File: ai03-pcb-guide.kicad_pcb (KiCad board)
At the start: 2 copper layers, 169.9 x 69.8 mm, 34 parts, among them J1 USB_mini_micro_B, SW1 SW_Push, U1 ATmega32U4-AU, Y1 Crystal_GND24_Small

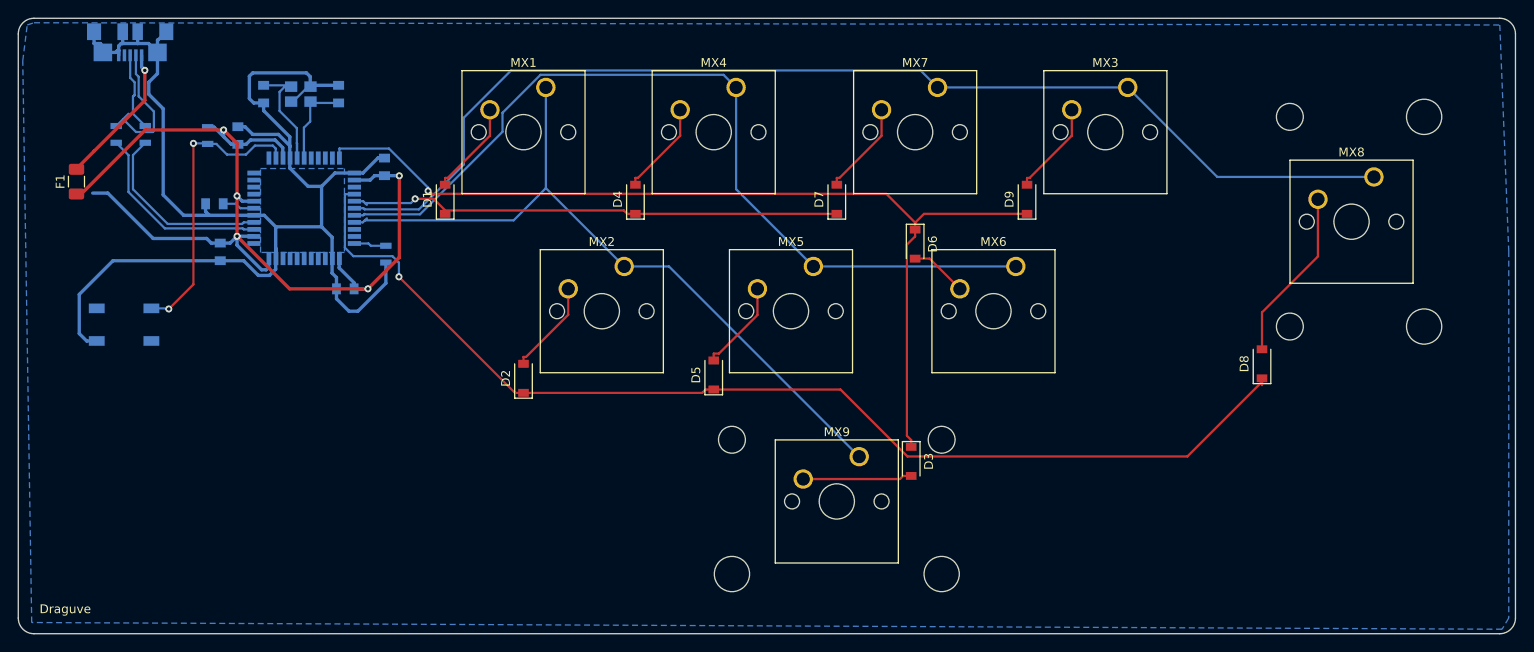
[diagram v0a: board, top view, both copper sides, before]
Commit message: using pro micro instead,added tht diodes,firmware
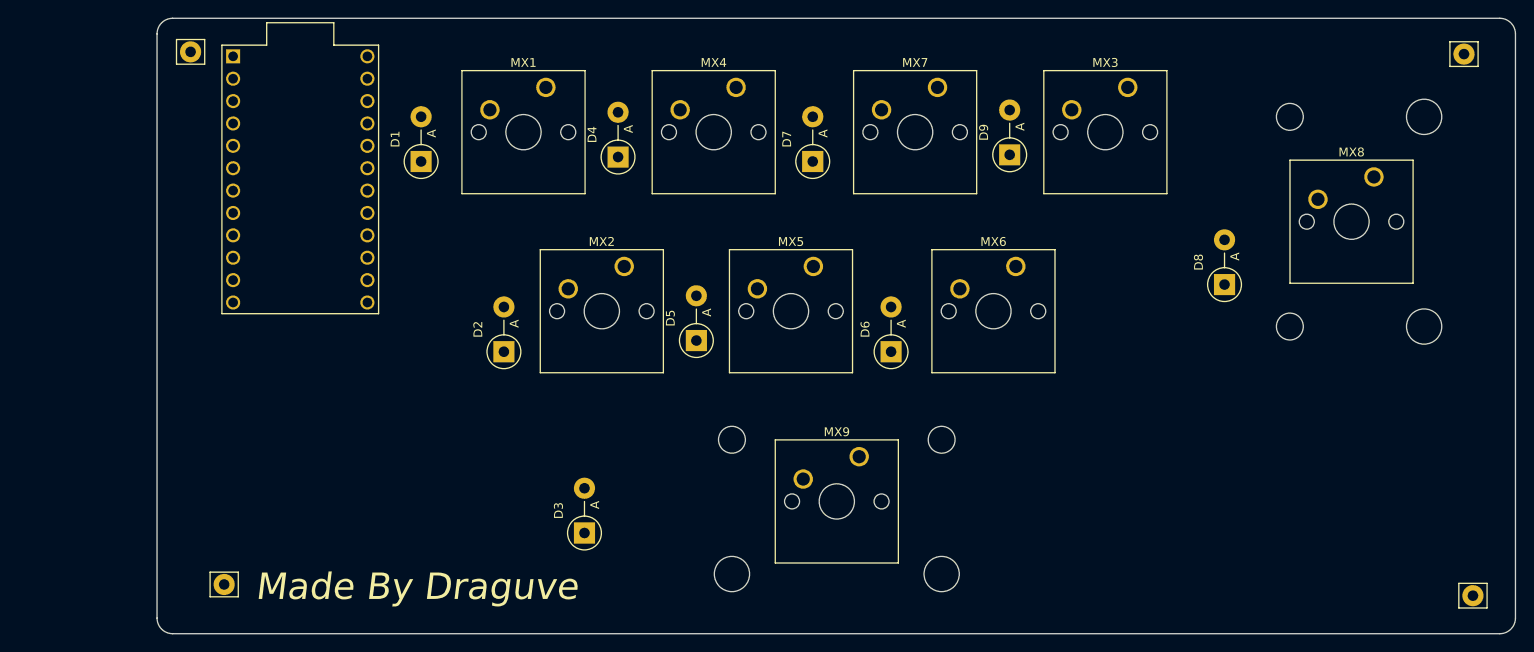
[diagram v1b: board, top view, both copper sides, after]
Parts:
- removed C1, C2, C5: 0.1uF, Capacitors_SMD:C_0805
- removed C3, C4: 22pF, Capacitors_SMD:C_0805
- removed C6: 1uF, Capacitors_SMD:C_0805
- removed C7: 10uF, Capacitors_SMD:C_0805
- removed F1: 500mA, Fuse:Fuse_1206_3216Metric
- removed J1: USB_mini_micro_B, keyboard_parts:USB_microB
- removed R1, R2: 22, Resistors_SMD:R_0805
- removed R3, R4: 10k, Resistors_SMD:R_0805
- removed SW1: SW_Push, random-keyboard-parts:SKQG-1155865
- removed Y1: Crystal_GND24_Small, Crystals:Crystal_SMD_3225-4pin_3.2x2.5mm
- added ?: , Connector_Pin:Pin_D1.2mm_L11.3mm_W3.0mm_Flat, F.Cu at (190.6, 64.8)
- added ?: , Connector_Pin:Pin_D1.2mm_L11.3mm_W3.0mm_Flat, F.Cu at (191.6, 126.3)
- added ?: , Connector_Pin:Pin_D1.2mm_L11.3mm_W3.0mm_Flat, F.Cu at (49.8, 125.0)
- added ?: , Connector_Pin:Pin_D1.2mm_L11.3mm_W3.0mm_Flat, F.Cu at (46.0, 64.5)
- D1, D2, D3, D4, D5, D6, D7, D8, D9: footprint Diode_SMD:D_SOD-123 -> Diode_THT:D_DO-15_P5.08mm_Vertical_AnodeUp
- U1: value ATmega32U4-AU -> ProMicro; footprint Housings_QFP:TQFP-44_10x10mm_Pitch0.8mm -> promicro:ProMicro; moved to F.Cu
- moved D3 38.0 mm to (90.7, 119.2), turned to 90 degrees
- moved D6 12.5 mm to (125.5, 98.6), turned to 90 degrees
- moved D8 9.95 mm to (163.4, 91.0)
- moved D9 5.42 mm to (139.0, 76.2)
- moved D4 5.19 mm to (94.6, 76.5)
- moved D1 5.09 mm to (72.2, 77.0)
- moved D7 5.09 mm to (116.6, 77.0)
- moved D5 4.38 mm to (103.4, 97.3)
- moved D2 3.75 mm to (81.6, 98.6)
- moved U1 3.30 mm to (58.5, 79.0), turned to 270 degrees
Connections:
- U1 pad 14: +5V -> COL2
- U1 pad 15: GND -> COL1
- U1 pad 16: Net-(C4-Pad1) -> COL0
- U1 pad 18: Net-(U1-Pad18) -> ROW2
- U1 pad 19: Net-(U1-Pad19) -> ROW1
- U1 pad 2: +5V -> Net-(U1-Pad2)
- U1 pad 20: Net-(U1-Pad20) -> ROW0
- U1 pad 22: ROW2 -> Net-(U1-Pad22)
- U1 pad 23: GND -> Net-(U1-Pad23)
- U1 pad 24: +5V -> Net-(U1-Pad24)
- U1 pad 5: GND -> Net-(U1-Pad5)
- U1 pad 7: +5V -> Net-(U1-Pad7)
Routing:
- net GND: track 163.8 -> 0.00 mm
- net COL2: track 130.4 -> 0.00 mm
- net ROW1: track 126.6 -> 0.00 mm, vias 1 -> 0
- net +5V: track 118.6 -> 0.00 mm, vias 5 -> 0
- net ROW2: track 109.3 -> 0.00 mm, vias 1 -> 0
- net COL1: track 98.8 -> 0.00 mm
- net COL0: track 83.3 -> 0.00 mm
- net ROW0: track 56.5 -> 0.00 mm, vias 1 -> 0
- net Net-(U1-Pad13): track 34.0 -> 0.00 mm, vias 2 -> 0
- net Net-(U1-Pad3): track 22.2 -> 0.00 mm
- net Net-(U1-Pad4): track 21.3 -> 0.00 mm
- net Net-(D8-Pad2): track 19.7 -> 0.00 mm
- net VCC: track 16.3 -> 0.00 mm, vias 1 -> 0
- net D-: track 15.6 -> 0.00 mm
- net Net-(C4-Pad1): track 14.8 -> 0.00 mm
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- removed copper zone on B.Cu, net GND
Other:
- board size 169.9 x 69.8 mm -> 154.2 x 69.8 mm
- board text added: "Made By Draguve"
- board text removed: "Draguve"

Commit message: Fixed stuff
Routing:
- net COL2: track 0.00 -> 127.5 mm
- net ROW2: track 0.00 -> 127.4 mm
- net ROW1: track 0.00 -> 118.3 mm
- net COL1: track 0.00 -> 94.0 mm
- net COL0: track 0.00 -> 82.1 mm
- net ROW0: track 0.00 -> 51.7 mm
- net Net-(D3-Pad2): track 0.00 -> 25.3 mm
- net Net-(D8-Pad2): track 0.00 -> 12.5 mm
- net Net-(D6-Pad2): track 0.00 -> 8.66 mm
- net Net-(D2-Pad2): track 0.00 -> 8.16 mm
- net Net-(D1-Pad2): track 0.00 -> 8.14 mm
- net Net-(D7-Pad2): track 0.00 -> 8.14 mm
- net Net-(D5-Pad2): track 0.00 -> 7.26 mm
- net Net-(D4-Pad2): track 0.00 -> 7.17 mm
- net Net-(D9-Pad2): track 0.00 -> 7.06 mm
